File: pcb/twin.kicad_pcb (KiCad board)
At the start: 4 copper layers, 78 x 72.8 mm, 68 parts, among them J1 USB_C_Receptacle_USB2.0_16P, SW1 RotaryEncoder_Switch, SW10 SW_Push_45deg, SW11 SW_Push_45deg, SW12 SW_Push_45deg, SW2 SW_Push_45deg, SW3 SW_Push_45deg, SW4 SW_Push_45deg, SW5 SW_Push_45deg, SW6 SW_Push_45deg, SW7 SW_Push_45deg, SW8 SW_Push_45deg, SW9 SW_Push_45deg, U1 ESP32-C6-MINI-1, U2 RP2040

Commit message: update pcb
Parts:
- added C13: 10uf, Capacitor_SMD:C_0603_1608Metric, F.Cu at (138.9, 93.8)
- added C14: 10uf, Capacitor_SMD:C_0603_1608Metric, F.Cu at (138.9, 96.3)
- added C15: 33pf, Capacitor_SMD:C_0603_1608Metric, F.Cu at (138.9, 98.8)
- added C16: 33pf, Capacitor_SMD:C_0603_1608Metric, F.Cu at (138.9, 101.3)
- added C17: 0.1uf, Capacitor_SMD:C_0603_1608Metric, F.Cu at (138.9, 103.8)
- added R3: 27, Resistor_SMD:R_0603_1608Metric, F.Cu at (142.9, 93.8)
- added R4: 27, Resistor_SMD:R_0603_1608Metric, F.Cu at (142.9, 96.3)
- added R5: 1k, Resistor_SMD:R_0603_1608Metric, F.Cu at (142.9, 98.8)
- added R6: 1k, Resistor_SMD:R_0603_1608Metric, F.Cu at (142.9, 101.3)
- added R7: 10k, Resistor_SMD:R_0603_1608Metric, F.Cu at (142.9, 103.8)
- added U3: MCP1700x-300xxTT, Package_TO_SOT_SMD:SOT-23, F.Cu at (147.3, 101.7)
- added U4: W25Q16JVSS, Package_SO:SOIC-8_5.3x5.3mm_P1.27mm, B.Cu at (62.2, 68.6)
- moved C11 53.4 mm to (161.1, 93.9)
- moved C6 53.4 mm to (161.1, 103.9)
- moved C8 53.4 mm to (161.1, 98.9)
- moved C9 53.4 mm to (161.1, 96.4)
- moved C7 53.4 mm to (161.1, 101.4)
- moved C1 53.4 mm to (157.1, 96.4)
- moved C10 53.4 mm to (157.1, 103.9)
- moved C12 53.4 mm to (165.1, 96.4)
- moved C2 53.4 mm to (157.1, 93.9)
- moved C3 53.4 mm to (157.1, 98.9)
- moved C5 53.4 mm to (165.1, 93.9)
- moved R1 53.4 mm to (165.1, 98.9)
- moved C4 53.4 mm to (157.1, 101.4)
- moved R2 53.4 mm to (165.1, 101.4)
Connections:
- J1 pad A4: +5V -> VBUS
- J1 pad A9: +5V -> VBUS
- J1 pad B4: +5V -> VBUS
- J1 pad B9: +5V -> VBUS
- SW1 pad A: unconnected-(SW1-PadA) -> /1A
- SW1 pad B: unconnected-(SW1-PadB) -> /1B
- SW1 pad C: unconnected-(SW1-PadC) -> GND
- U2 pad 19: unconnected-(U2-TESTEN-Pad19) -> GND
- U2 pad 46: /D- -> Net-(U2-USB_DM)
- U2 pad 47: /D+ -> Net-(U2-USB_DP)
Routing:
- net /QSPI_SD0: track 0.00 -> 10.1 mm
- net /QSPI_SCLK: track 0.00 -> 8.29 mm
- net +5V: track 16.4 -> 9.64 mm, vias 15 -> 14
- net VBUS: track 0.00 -> 6.72 mm, vias 0 -> 1
- net /QSPI_SD3: track 0.00 -> 5.62 mm
- net +3V3: track 25.9 -> 31.1 mm, vias 0 -> 2

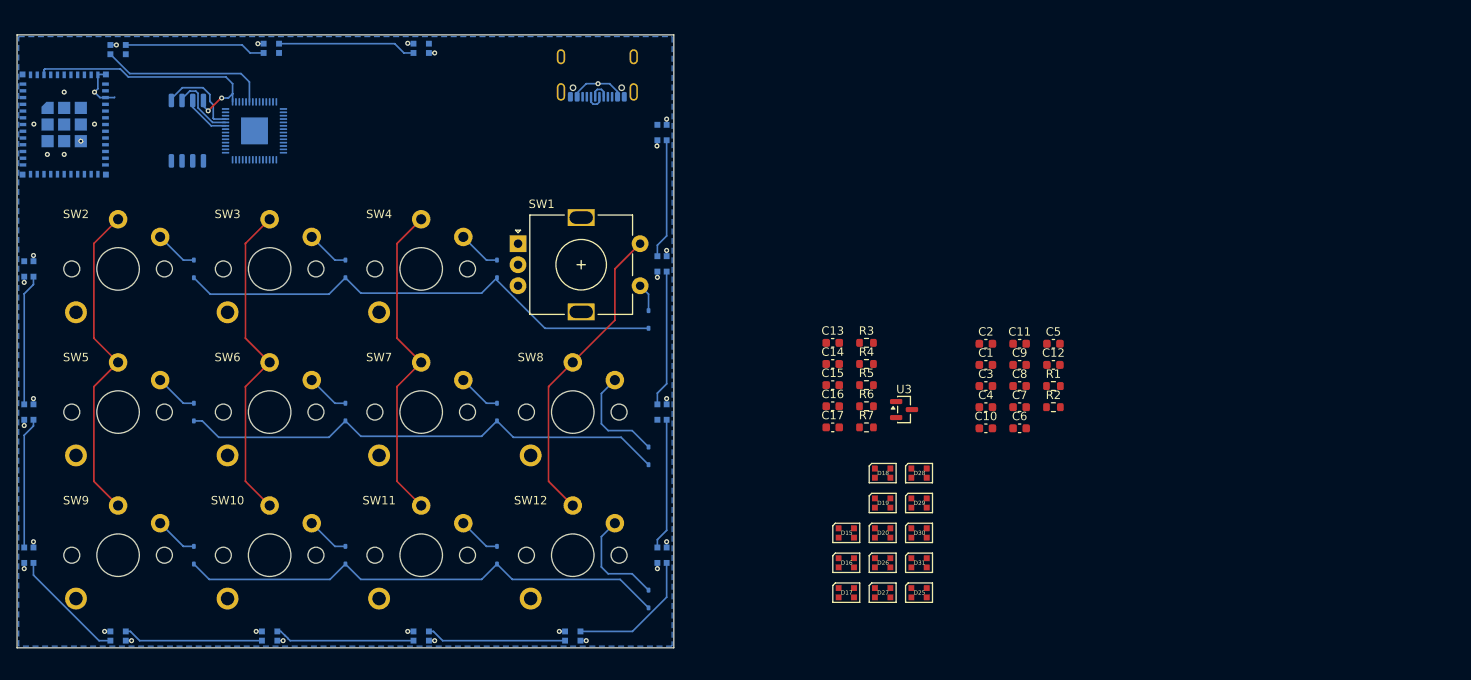
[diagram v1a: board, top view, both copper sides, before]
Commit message: Update PCB footprints and backups
Clean up PCB repository and update the board file. Removed macOS .DS_Store and a stale KiCad schematic lock, rotated twin-backups (deleted older backup zips and added new ones). Large edits to pcb/twin.kicad_pcb: reorganized net names, replaced/updated multiple footprints (added Choc keyswitch and Alps rotary encoder footprints, changed capacitor footprints/sizes, converted several pads from SMD to thru-hole), and updated 3D model paths and footprint metadata to match recent hardware/layout changes.
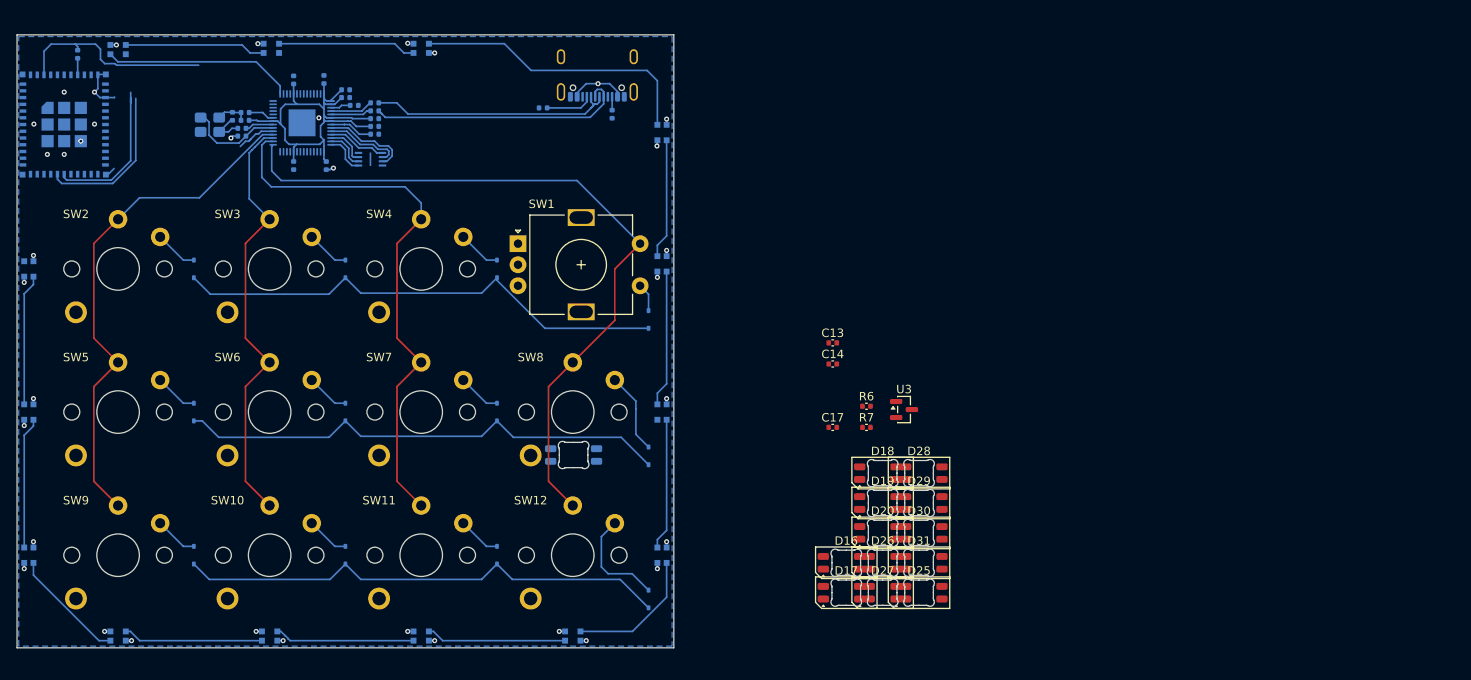
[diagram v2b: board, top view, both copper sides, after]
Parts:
- added R8: 10k, Capacitor_SMD:C_0402_1005Metric, B.Cu at (49.2, 59.5)
- added Y1: 12MHz, Crystal:Crystal_SMD_3225-4Pin_3.2x2.5mm, B.Cu at (64.9, 67.9)
- C1, C10, C11, C12, C15, C16, C2, C3, C4, C5, C6, C7, C8, C9: footprint Capacitor_SMD:C_0603_1608Metric -> Capacitor_SMD:C_0402_1005Metric; moved to B.Cu
- C13, C14, C17: footprint Capacitor_SMD:C_0603_1608Metric -> Capacitor_SMD:C_0402_1005Metric
- D15: footprint LED_SMD:LED_WS2812B-2020_PLCC4_2.0x2.0mm -> LED_SMD:LED_SK6812MINI-E_3.2x2.8mm_P1.5mm_ReverseMount; moved to B.Cu
- D16, D17, D18, D19, D20, D25, D26, D27, D28, D29, D30, D31: footprint LED_SMD:LED_WS2812B-2020_PLCC4_2.0x2.0mm -> LED_SMD:LED_SK6812MINI-E_3.2x2.8mm_P1.5mm_ReverseMount
- R1, R2, R3, R4, R5: footprint Resistor_SMD:R_0603_1608Metric -> Capacitor_SMD:C_0402_1005Metric; moved to B.Cu
- R6, R7: footprint Resistor_SMD:R_0603_1608Metric -> Capacitor_SMD:C_0402_1005Metric
- U4: footprint Package_SO:SOIC-8_5.3x5.3mm_P1.27mm -> Package_SON:Winbond_USON-8-1EP_3x2mm_P0.5mm_EP0.2x1.6mm
- moved C8 97.3 mm to (69.1, 67.3), turned to 180 degrees
- moved C7 94.6 mm to (74.8, 62.5), turned to 90 degrees
- moved C3 93.8 mm to (69.1, 66.4), turned to 180 degrees
- moved C6 92.4 mm to (78.5, 62.5), turned to 90 degrees
- moved C12 89.9 mm to (81.0, 64.7)
- moved C9 89.4 mm to (74.8, 72.7), turned to -90 degrees
- moved C5 89.3 mm to (81.0, 63.7)
- moved C10 84.3 mm to (78.7, 72.7), turned to -90 degrees
- moved C11 81.1 mm to (84.5, 67.2)
- moved R5 80.2 mm to (68.7, 68.3)
- moved C2 80.2 mm to (82.0, 65.6)
- moved C4 79.9 mm to (84.5, 68.1)
- moved C16 79.2 mm to (67.6, 66.9), turned to -90 degrees
- moved C1 77.6 mm to (84.5, 69.0)
- moved C15 76.1 mm to (68.7, 69.2)
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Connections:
- C14 pad 1: VBUS -> +5V
- J1 pad A4: VBUS -> +5V
- J1 pad A9: VBUS -> +5V
- J1 pad B4: VBUS -> +5V
- J1 pad B9: VBUS -> +5V
- U1 pad 10: unconnected-(U1-IO5-Pad10) -> /ESP-SDA
- U1 pad 8: unconnected-(U1-EN-Pad8) -> Net-(U1-EN)
- U1 pad 9: unconnected-(U1-IO4-Pad9) -> /ESP-SCL
- U2 pad 13: /r1 -> unconnected-(U2-GPIO10-Pad13)
- U2 pad 14: /r2 -> unconnected-(U2-GPIO11-Pad14)
- U2 pad 15: /r3 -> /c4
- U2 pad 16: unconnected-(U2-GPIO13-Pad16) -> /c3
- U2 pad 17: unconnected-(U2-GPIO14-Pad17) -> /c2
- U2 pad 18: unconnected-(U2-GPIO15-Pad18) -> /c1
- U2 pad 2: unconnected-(U2-GPIO0-Pad2) -> /ESP-TX
- U2 pad 29: unconnected-(U2-GPIO18-Pad29) -> /backlight
- U2 pad 3: unconnected-(U2-GPIO1-Pad3) -> /ESP-RX
- U2 pad 34: /c4 -> unconnected-(U2-GPIO22-Pad34)
- U2 pad 35: /c3 -> unconnected-(U2-GPIO23-Pad35)
- U2 pad 36: /c2 -> unconnected-(U2-GPIO24-Pad36)
- U2 pad 37: /c1 -> unconnected-(U2-GPIO25-Pad37)
- U2 pad 38: unconnected-(U2-GPIO26_ADC0-Pad38) -> /r1
- U2 pad 39: unconnected-(U2-GPIO27_ADC1-Pad39) -> /r2
- U2 pad 40: unconnected-(U2-GPIO28_ADC2-Pad40) -> /r3
- U2 pad 6: /backlight -> unconnected-(U2-GPIO4-Pad6)
- U3 pad 3: VBUS -> +5V
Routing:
- net /c4: track 36.8 -> 87.3 mm
- net +3V3: track 31.1 -> 74.5 mm, vias 2 -> 0
- net Net-(D3-DOUT): track 0.00 -> 34.2 mm
- net /D+: track 2.45 -> 31.0 mm
- net /c3: track 38.8 -> 66.2 mm
- net /D-: track 2.44 -> 29.8 mm
- net /c1: track 38.8 -> 61.3 mm
- net /ESP-TX: track 0.00 -> 18.6 mm
- net /ESP-RX: track 0.00 -> 18.2 mm
- net /c2: track 38.8 -> 51.2 mm
- net GND: track 13.4 -> 25.0 mm, vias 18 -> 21
- net /XIN: track 0.00 -> 11.0 mm
- net +1V1: track 0.00 -> 10.7 mm
- net +5V: track 9.64 -> 16.4 mm, vias 14 -> 15
- net VBUS: track 6.72 -> 0.00 mm, vias 1 -> 0
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
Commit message: s
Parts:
- removed the D15 at (108.1, 107.1)
- removed the D16 at (140.5, 119.9)
- removed the D17 at (140.5, 123.5)
- removed the D18 at (144.8, 109.2)
- removed the D19 at (144.8, 112.8)
- removed the D20 at (144.8, 116.3)
- removed the D29 at (149.1, 112.8)
- removed the D30 at (149.1, 116.3)
- removed the D31 at (149.1, 119.9)
- added D23: LED_SK6812MINI, footprints:MX_SK6812MINI-E, F.Cu at (90.0, 85.0)
- added D24: LED_SK6812MINI, footprints:MX_SK6812MINI-E, F.Cu at (72.0, 85.0)
- added D34: LED_SK6812MINI, footprints:MX_SK6812MINI-E, F.Cu at (54.0, 119.0)
- added D35: LED_SK6812MINI, footprints:MX_SK6812MINI-E, F.Cu at (72.0, 119.0)
- added D36: LED_SK6812MINI, footprints:MX_SK6812MINI-E, F.Cu at (90.0, 119.0)
- added D37: LED_SK6812MINI, footprints:MX_SK6812MINI-E, F.Cu at (108.0, 119.0)
- added D38: LED_SK6812MINI, footprints:MX_SK6812MINI-E, F.Cu at (108.0, 102.0)
- added SW1: SW_Push, Button_Switch_SMD:SW_Push_SPST_NO_Alps_SKRK, F.Cu at (130.0, 76.4)
- added SW2: SW_Push, Button_Switch_SMD:SW_Push_SPST_NO_Alps_SKRK, F.Cu at (130.0, 72.0)
- D10: renamed from D23; footprint Diode_SMD:D_SOD-323 -> Diode_SMD:D_SOD-323_HandSoldering
- D11: renamed from D24; footprint Diode_SMD:D_SOD-323 -> Diode_SMD:D_SOD-323_HandSoldering
- D19: renamed from D32; footprint Diode_SMD:D_SOD-323 -> Diode_SMD:D_SOD-323_HandSoldering
- D20: renamed from D33; footprint Diode_SMD:D_SOD-323 -> Diode_SMD:D_SOD-323_HandSoldering
- D21: renamed from D34; footprint Diode_SMD:D_SOD-323 -> Diode_SMD:D_SOD-323_HandSoldering
- D22: renamed from D35; footprint Diode_SMD:D_SOD-323 -> Diode_SMD:D_SOD-323_HandSoldering
- D25, D26, D27, D28: value WS2812B-2020 -> LED_SK6812MINI; footprint LED_SMD:LED_SK6812MINI-E_3.2x2.8mm_P1.5mm_ReverseMount -> footprints:MX_SK6812MINI-E
- D29: renamed from D36; footprint Diode_SMD:D_SOD-323 -> Diode_SMD:D_SOD-323_HandSoldering
- D30: renamed from D37; footprint Diode_SMD:D_SOD-323 -> Diode_SMD:D_SOD-323_HandSoldering
- D31: renamed from D38; footprint Diode_SMD:D_SOD-323 -> Diode_SMD:D_SOD-323_HandSoldering
- D32: renamed from D39; footprint Diode_SMD:D_SOD-323 -> Diode_SMD:D_SOD-323_HandSoldering
- D8: renamed from D21; footprint Diode_SMD:D_SOD-323 -> Diode_SMD:D_SOD-323_HandSoldering
- D9: renamed from D22; footprint Diode_SMD:D_SOD-323 -> Diode_SMD:D_SOD-323_HandSoldering
- moved D25 102.6 mm to (54.0, 85.0)
- moved D26 92.6 mm to (54.0, 102.0)
- moved D27 75.9 mm to (72.0, 102.0)
- moved D28 59.6 mm to (90.0, 102.0)
- renumbered C14 to C13, C13 to C14, D8 to D12, D9 to D13, D10 to D14, D11 to D15, D12 to D16, D13 to D17, D14 to D18, R8 to R1, R1 to R2, R2 to R3, R3 to R4, R4 to R5, R5 to R6, R6 to R8, SW8 to SW10, SW9 to SW11, SW10 to SW12, SW11 to SW13, SW12 to SW14, SW1 to SW3, SW2 to SW4, SW3 to SW5, SW4 to SW6, SW5 to SW7, SW6 to SW8, SW7 to SW9, U3 to U1, U1 to U2, U2 to U3
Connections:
- D25 pad 1: unconnected-(D25-DOUT-Pad1) -> +5V
- D25 pad 2: GND -> Net-(D25-DOUT)
- D25 pad 3: Net-(D25-DIN) -> GND
- D25 pad 4: +5V -> Net-(D24-DOUT)
- D26 pad 1: Net-(D25-DIN) -> +5V
- D26 pad 2: GND -> Net-(D26-DOUT)
- D26 pad 3: Net-(D26-DIN) -> GND
- D26 pad 4: +5V -> Net-(D25-DOUT)
- D27 pad 1: Net-(D26-DIN) -> +5V
- D27 pad 2: GND -> Net-(D27-DOUT)
- D27 pad 3: Net-(D27-DIN) -> GND
- D27 pad 4: +5V -> Net-(D26-DOUT)
- D28 pad 1: Net-(D27-DIN) -> +5V
- D28 pad 2: GND -> Net-(D28-DOUT)
- D28 pad 3: Net-(D28-DIN) -> GND
- D28 pad 4: +5V -> Net-(D27-DOUT)
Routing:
- net /r3: track 59.2 -> 86.8 mm
- net /r2: track 59.3 -> 84.7 mm
- net /ESP-TX: track 18.6 -> 0.00 mm
- net /ESP-RX: track 18.2 -> 0.00 mm
- net +3V3: track 74.5 -> 57.6 mm
- net /r1: track 59.8 -> 74.1 mm
- net Net-(D32-A): track 12.6 -> 9.61 mm
- net GND: track 25.0 -> 22.5 mm, vias 21 -> 22
- net /c4: track 87.3 -> 88.8 mm, vias 0 -> 1
- net Net-(D14-DIN): track 13.8 -> 14.9 mm
- net /c3: track 66.2 -> 66.5 mm, vias 0 -> 1
- net /c2: track 51.2 -> 51.5 mm, vias 0 -> 1
- net /c1: track 61.3 -> 61.5 mm, vias 0 -> 1

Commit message: loads of stuff
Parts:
- added C18: 100nf, Capacitor_SMD:C_0402_1005Metric, B.Cu at (104.0, 82.0)
- added C19: 100nf, Capacitor_SMD:C_0402_1005Metric, B.Cu at (104.2, 87.0)
- added C20: 1uf, Capacitor_SMD:C_0402_1005Metric, B.Cu at (45.8, 60.0)
- added C21: 100nf, Capacitor_SMD:C_0402_1005Metric, B.Cu at (46.9, 59.9)
- added C22: 100nf, Capacitor_SMD:C_0402_1005Metric, B.Cu at (54.6, 73.5)
- added C23: 100nf, Capacitor_SMD:C_0402_1005Metric, B.Cu at (54.1, 63.5)
- added G***: LOGO, LOGO, B.Cu at (47.2, 112.9)
- added H1: MountingHole_Pad, MountingHole:MountingHole_2.2mm_M2_DIN965_Pad, F.Cu at (63.0, 75.5)
- added H2: MountingHole_Pad, MountingHole:MountingHole_2.2mm_M2_DIN965_Pad, F.Cu at (99.5, 75.5)
- added H3: MountingHole_Pad, MountingHole:MountingHole_2.2mm_M2_DIN965_Pad, F.Cu at (63.0, 110.5)
- added H4: MountingHole_Pad, MountingHole:MountingHole_2.2mm_M2_DIN965_Pad, F.Cu at (99.0, 110.5)
- added J2: ESP FLASH, Connector_PinHeader_2.54mm:PinHeader_1x04_P2.54mm_Vertical, B.Cu at (44.0, 89.7)
- added R10: 10k, Capacitor_SMD:C_0402_1005Metric, B.Cu at (54.7, 69.3)
- added R11: 47, Capacitor_SMD:C_0402_1005Metric, B.Cu at (49.2, 76.3)
- added R12: 47, Capacitor_SMD:C_0402_1005Metric, B.Cu at (49.2, 75.2)
- added R13: 10k, Capacitor_SMD:C_0402_1005Metric, B.Cu at (67.5, 65.4)
- added R9: 10k, Capacitor_SMD:C_0402_1005Metric, B.Cu at (54.7, 71.2)
- added SW15: BOOT, Button_Switch_SMD:SW_Push_SPST_NO_Alps_SKRK, B.Cu at (58.5, 71.8)
- added SW16: BOOT, Button_Switch_SMD:SW_Push_SPST_NO_Alps_SKRK, B.Cu at (68.3, 63.2)
- C13, C14, R7, R8, SW1, SW2: moved to B.Cu
- C17: value 0.1uf -> 100nf; moved to B.Cu
- SW10, SW11, SW12, SW13, SW14, SW4, SW5, SW6, SW7, SW8, SW9: value SW_Push_45deg -> Choc
- U1: value MCP1700x-300xxTT -> MCP1700x-330xxTT; moved to B.Cu
- moved SW1 73.7 mm to (57.5, 62.8), turned to 180 degrees
- moved R8 68.8 mm to (80.5, 72.3), turned to -45 degrees
- moved R7 67.3 mm to (82.7, 73.8)
- moved U1 61.2 mm to (98.7, 64.7)
- moved C17 60.3 mm to (87.3, 72.7)
- moved C14 52.4 mm to (95.3, 64.6), turned to 180 degrees
- moved C13 48.7 mm to (100.8, 65.9), turned to 180 degrees
- moved SW2 38.9 mm to (91.1, 70.0), turned to 180 degrees
- moved R2 1.01 mm to (103.9, 66.7)
- moved C6 0.32 mm to (78.8, 62.5)
- moved C9 0.31 mm to (74.7, 73.0)
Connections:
- U2 pad 22: unconnected-(U2-IO8-Pad22) -> Net-(U2-IO8)
- U2 pad 23: unconnected-(U2-IO9-Pad23) -> Net-(SW15-B)
- U2 pad 30: /ESP-RX -> Net-(U2-RXD0)
- U2 pad 31: /ESP-TX -> Net-(U2-TXD0)
- U3 pad 12: unconnected-(U3-GPIO9-Pad12) -> /r1
- U3 pad 13: unconnected-(U3-GPIO10-Pad13) -> /r2
- U3 pad 14: unconnected-(U3-GPIO11-Pad14) -> /r3
- U3 pad 26: unconnected-(U3-RUN-Pad26) -> Net-(SW16-B)
- U3 pad 38: /r1 -> unconnected-(U3-GPIO26_ADC0-Pad38)
- U3 pad 39: /r2 -> unconnected-(U3-GPIO27_ADC1-Pad39)
- U3 pad 40: /r3 -> unconnected-(U3-GPIO28_ADC2-Pad40)
- U3 pad 7: /underswitch -> /1A
- U3 pad 8: unconnected-(U3-GPIO6-Pad8) -> /1B
- U3 pad 9: unconnected-(U3-GPIO7-Pad9) -> /underswitch
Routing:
- net +3V3: track 57.6 -> 164.7 mm, vias 0 -> 5
- net /ESP-RX: track 0.00 -> 54.0 mm, vias 0 -> 4
- net /ESP-TX: track 0.00 -> 52.9 mm, vias 0 -> 2
- net /r3: track 86.8 -> 132.1 mm, vias 0 -> 2
- net +5V: track 16.4 -> 53.4 mm, vias 15 -> 26
- net /1B: track 0.00 -> 36.5 mm
- net /underswitch: track 0.00 -> 36.1 mm, vias 0 -> 2
- net /r2: track 84.7 -> 118.9 mm, vias 0 -> 2
- net Net-(D28-DOUT): track 0.00 -> 33.4 mm
- net Net-(D26-DOUT): track 0.00 -> 33.0 mm, vias 0 -> 2
- net /1A: track 0.00 -> 32.5 mm
- net Net-(D27-DOUT): track 0.00 -> 32.4 mm, vias 0 -> 2
- net GND: track 22.5 -> 44.1 mm, vias 22 -> 64
- net +1V1: track 10.7 -> 31.5 mm, vias 0 -> 3
- net /r1: track 74.1 -> 93.4 mm
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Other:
- board text added: "+3V3"
- board text added: "Boot"
- board text added: "EN"
- board text added: "ESP32"
- board text added: "GND"
- board text added: "RP2040"
- board text added: "RX"
- board text added: "Reset"
- board text added: "TX"
- board text added: "USB-C"
- board text added: "twin"
- board text added: "vejas.zip"
- board text added: "ツイン"
